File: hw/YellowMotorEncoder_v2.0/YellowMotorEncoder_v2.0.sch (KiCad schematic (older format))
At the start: 30 parts, among them J1 Conn_01x06, Q1 AO3401A, U1 47k, U10 10k, U11 47k, U12 18p/50V, U13 BLUE, U14 10k, U15 BLUE, U16 10k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

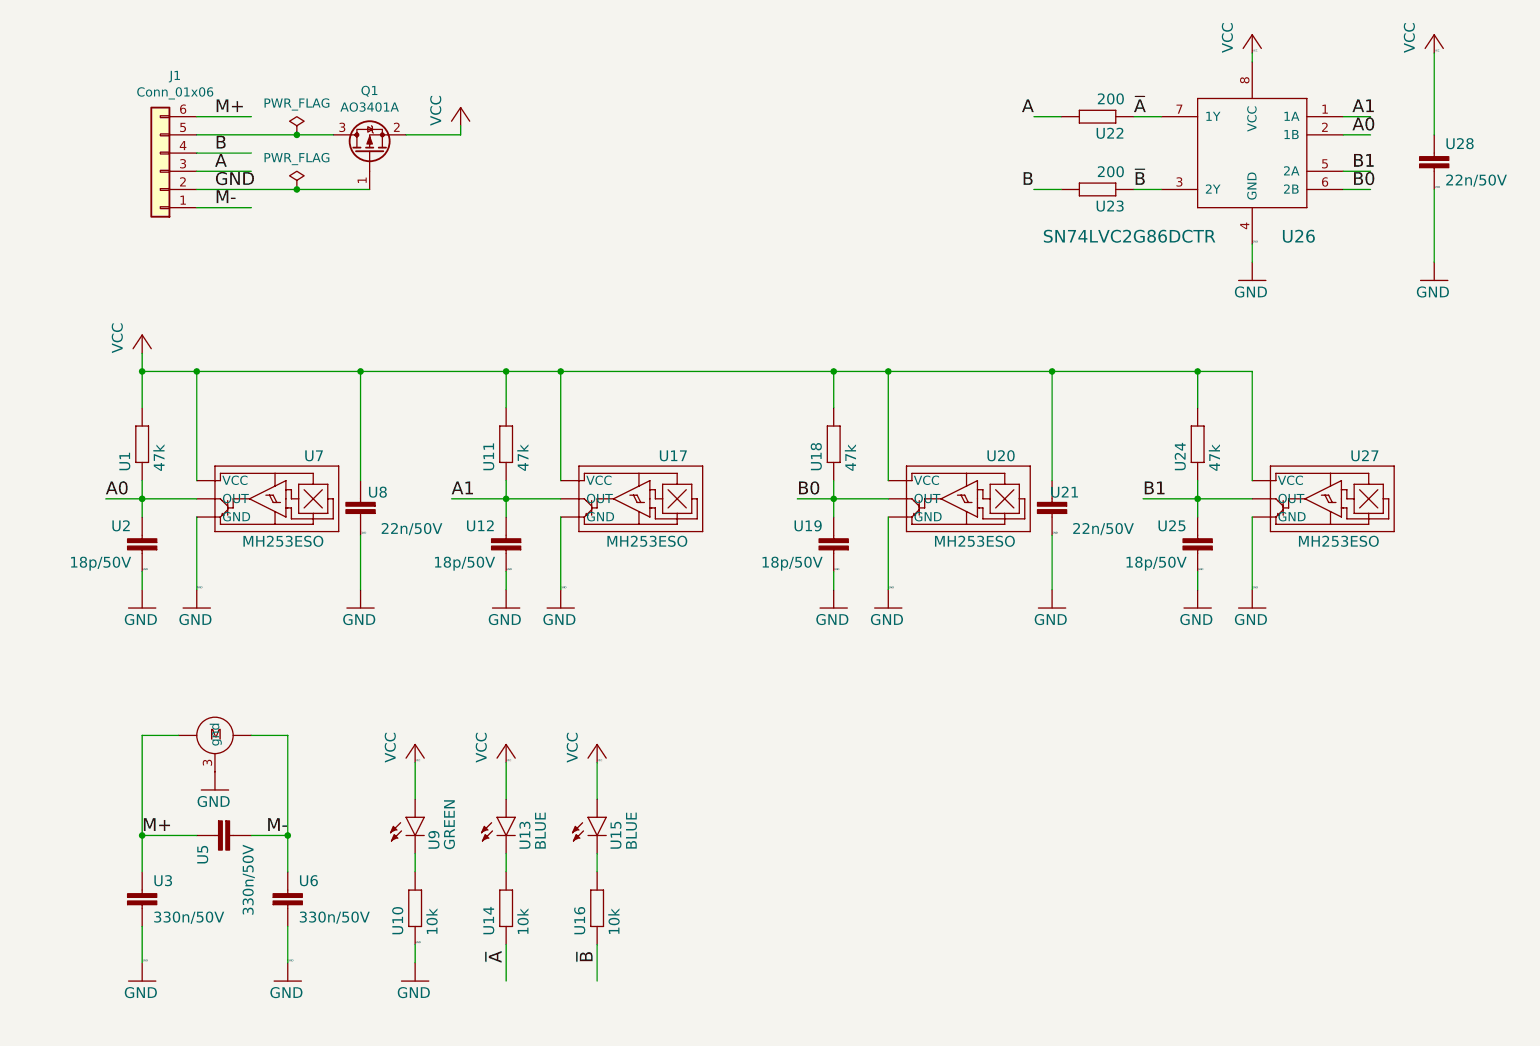
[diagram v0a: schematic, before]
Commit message: 3D_viewer
i add 3d model of motor and connector
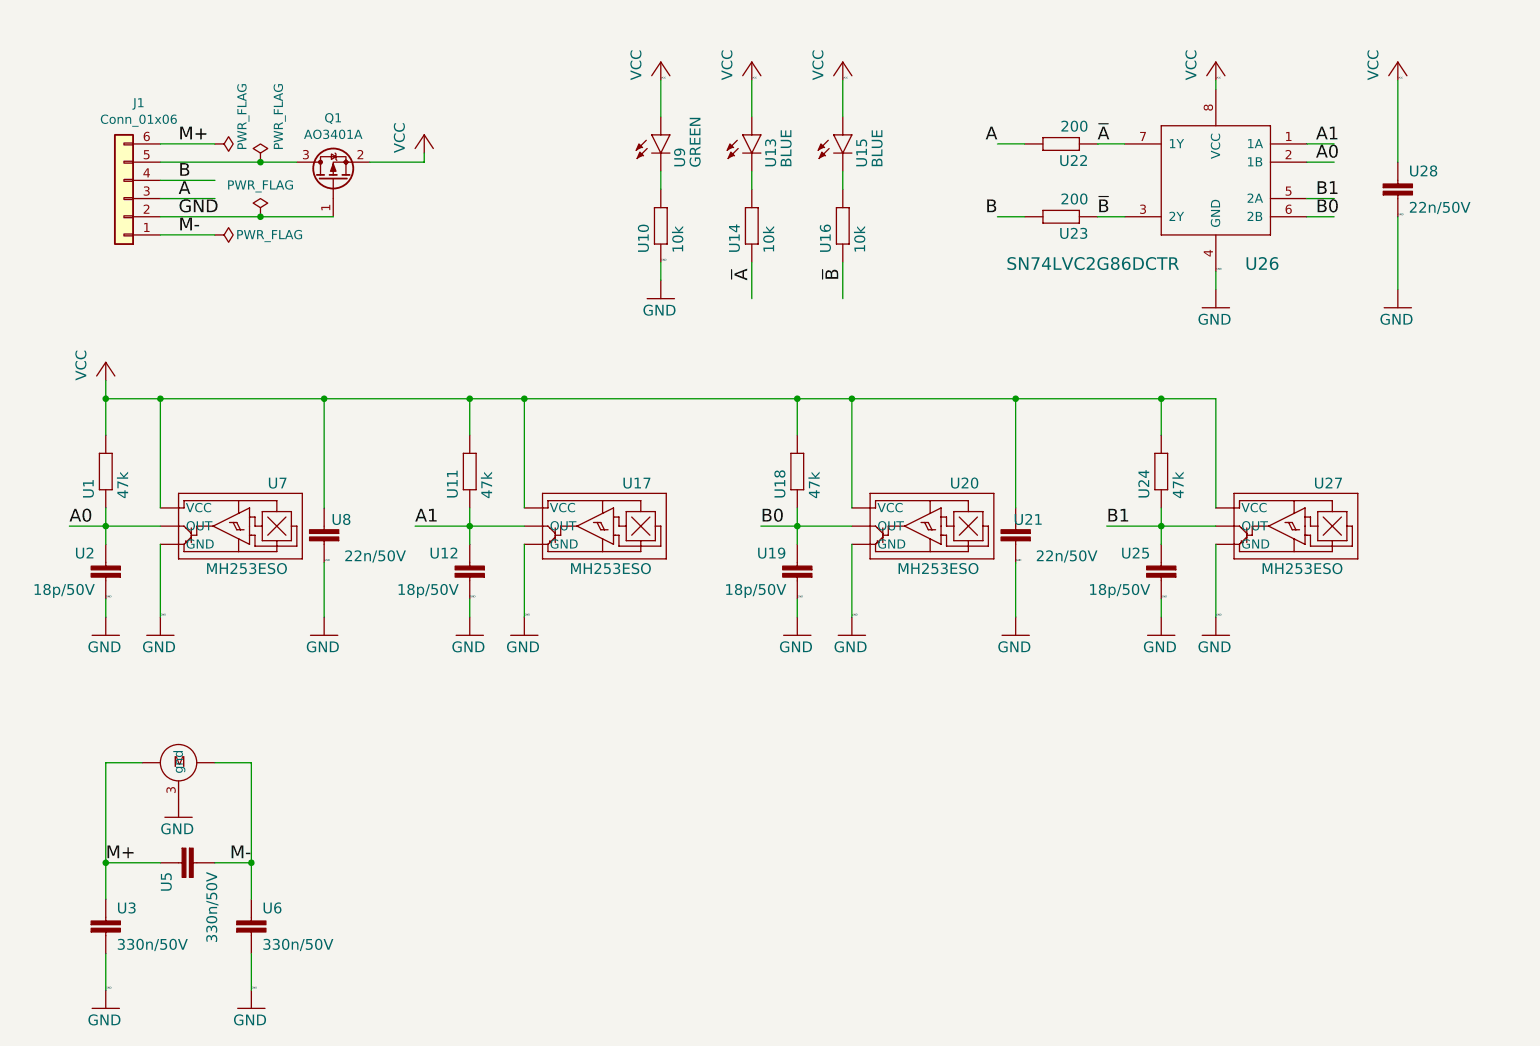
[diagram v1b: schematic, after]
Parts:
- U7: LCSC (none) -> C114369
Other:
- moved on the sheet: J1, Q1, U1, U10, U11, U12, U13, U14, U15, U16, U17, U18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

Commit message: rotate sensors
I changing position of sensors and rotating it in circle around hole for shaft of motor.
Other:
- moved on the sheet: U11, U12, U17, U18, U19, U20, U24, U25, U27
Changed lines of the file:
@@
 Wire Wire Line
 	6200 3950 6200 3850
-Wire Wire Line
-	6200 4050 6200 3950
 Text Label 6000 3950 0    70   ~ 0
 B0
@@
 L YellowMotorEncoder_v2.0-eagle-import:MH253ESO U27
 U 1 1 5F83AED4
-P 9100 3950
-F 0 "U27" H 9000 4150 59  0000 L BNN
-F 1 "MH253ESO" H 9000 3680 59  0000 L BNN
-F 2 "Package_TO_SOT_SMD:SOT-23" H 9100 3950 50  0001 C CNN
-F 3 "" H 9100 3950 50  0001 C CNN
-	1    9100 3950
+P 7100 3950
+F 0 "U27" H 7000 4150 59  0000 L BNN
+F 1 "MH253ESO" H 7000 3680 59  0000 L BNN
+F 2 "Package_TO_SOT_SMD:SOT-23" H 7100 3950 50  0001 C CNN
+F 3 "" H 7100 3950 50  0001 C CNN
+	1    7100 3950
 	-1   0    0    -1
 $EndComp
@@
 L YellowMotorEncoder_v2.0-eagle-import:R-EU_R0402 U24
 U 1 1 5F8679BE
-P 8200 3650
-F 0 "U24" H 8050 3709 59  0000 L BNN
-F 1 "47k" H 8050 3520 59  0000 L BNN
-F 2 "Resistor_SMD:R_0402_1005Metric" H 8200 3650 50  0001 C CNN
-F 3 "" H 8200 3650 50  0001 C CNN
-F 4 "C25792" H 8200 3650 59  0001 L BNN "LCSC"
-	1    8200 3650
+P 6200 3650
+F 0 "U24" H 6050 3709 59  0000 L BNN
+F 1 "47k" H 6050 3520 59  0000 L BNN
+F 2 "Resistor_SMD:R_0402_1005Metric" H 6200 3650 50  0001 C CNN
+F 3 "" H 6200 3650 50  0001 C CNN
+F 4 "C25792" H 6200 3650 59  0001 L BNN "LCSC"
+	1    6200 3650
 	0    -1   -1   0
 $EndComp
@@
 L YellowMotorEncoder_v2.0-eagle-import:MH253ESO U20
 U 1 1 5F86AC81
-P 7100 3950
-F 0 "U20" H 7000 4150 59  0000 L BNN
-F 1 "MH253ESO" H 7000 3680 59  0000 L BNN
-F 2 "Package_TO_SOT_SMD:SOT-23" H 7100 3950 50  0001 C CNN
-F 3 "" H 7100 3950 50  0001 C CNN
-	1    7100 3950
-	-1   0    0    -1
-$EndComp
-$Comp
-L YellowMotorEncoder_v2.0-eagle-import:MH253ESO U17
-U 1 1 5F86BD7E
 P 5300 3950
-F 0 "U17" H 5200 4150 59  0000 L BNN
+F 0 "U20" H 5200 4150 59  0000 L BNN
 F 1 "MH253ESO" H 5200 3680 59  0000 L BNN
 F 2 "Package_TO_SOT_SMD:SOT-23" H 5300 3950 50  0001 C CNN
 F 3 "" H 5300 3950 50  0001 C CNN
 	1    5300 3950
+	-1   0    0    -1
+$EndComp
+$Comp
+L YellowMotorEncoder_v2.0-eagle-import:MH253ESO U17
+U 1 1 5F86BD7E
+P 9100 3950
+F 0 "U17" H 9000 4150 59  0000 L BNN
+F 1 "MH253ESO" H 9000 3680 59  0000 L BNN
+F 2 "Package_TO_SOT_SMD:SOT-23" H 9100 3950 50  0001 C CNN
+F 3 "" H 9100 3950 50  0001 C CNN
+	1    9100 3950
 	-1   0    0    -1
 $EndComp
@@
 L YellowMotorEncoder_v2.0-eagle-import:C-EUC0402 U12
 U 1 1 5F8749CE
+P 8200 4150
+F 0 "U12" H 8260 4165 59  0000 L BNN
+F 1 "18p/50V" H 8260 3965 59  0000 L BNN
+F 2 "Capacitor_SMD:C_0402_1005Metric" H 8200 4150 50  0001 C CNN
+F 3 "" H 8200 4150 50  0001 C CNN
+F 4 "C1549" H 8200 4150 59  0001 L BNN "LCSC"
+	1    8200 4150
+	-1   0    0    -1
+$EndComp
+$Comp
+L YellowMotorEncoder_v2.0-eagle-import:C-EUC0402 U19
+U 1 1 5F8754D9
 P 4400 4150
-F 0 "U12" H 4460 4165 59  0000 L BNN
+F 0 "U19" H 4460 4165 59  0000 L BNN
 F 1 "18p/50V" H 4460 3965 59  0000 L BNN
 F 2 "Capacitor_SMD:C_0402_1005Metric" H 4400 4150 50  0001 C CNN
@@
 F 4 "C1549" H 4400 4150 59  0001 L BNN "LCSC"
 	1    4400 4150
-	-1   0    0    -1
-$EndComp
-$Comp
-L YellowMotorEncoder_v2.0-eagle-import:C-EUC0402 U19
-U 1 1 5F8754D9
-P 6200 4150
-F 0 "U19" H 6260 4165 59  0000 L BNN
-F 1 "18p/50V" H 6260 3965 59  0000 L BNN
-F 2 "Capacitor_SMD:C_0402_1005Metric" H 6200 4150 50  0001 C CNN
-F 3 "" H 6200 4150 50  0001 C CNN
-F 4 "C1549" H 6200 4150 59  0001 L BNN "LCSC"
-	1    6200 4150
-	-1   0    0    -1
-$EndComp
-$Comp
-L YellowMotorEncoder_v2.0-eagle-import:C-EUC0402 U25
-U 1 1 5F876094
-P 8200 4150
-F 0 "U25" H 8260 4165 59  0000 L BNN
-F 1 "18p/50V" H 8260 3965 59  0000 L BNN
-F 2 "Capacitor_SMD:C_0402_1005Metric" H 8200 4150 50  0001 C CNN
-F 3 "" H 8200 4150 50  0001 C CNN
-F 4 "C1549" H 8200 4150 59  0001 L BNN "LCSC"
-	1    8200 4150
 	-1   0    0    -1
 $EndComp
@@
 L YellowMotorEncoder_v2.0-eagle-import:R-EU_R0402 U18
 U 1 1 5F8A9DF8
-P 6200 3650
-F 0 "U18" H 6050 3709 59  0000 L BNN
-F 1 "47k" H 6050 3520 59  0000 L BNN
-F 2 "Resistor_SMD:R_0402_1005Metric" H 6200 3650 50  0001 C CNN
-F 3 "" H 6200 3650 50  0001 C CNN
-F 4 "C25792" H 6200 3650 59  0001 L BNN "LCSC"
-	1    6200 3650
-	0    -1   -1   0
-$EndComp
-$Comp
-L YellowMotorEncoder_v2.0-eagle-import:R-EU_R0402 U11
-U 1 1 5F8AAAB3
 P 4400 3650
-F 0 "U11" H 4250 3709 59  0000 L BNN
+F 0 "U18" H 4250 3709 59  0000 L BNN
 F 1 "47k" H 4250 3520 59  0000 L BNN
 F 2 "Resistor_SMD:R_0402_1005Metric" H 4400 3650 50  0001 C CNN
@@
 F 4 "C25792" H 4400 3650 59  0001 L BNN "LCSC"
 	1    4400 3650
+	0    -1   -1   0
+$EndComp
+$Comp
+L YellowMotorEncoder_v2.0-eagle-import:R-EU_R0402 U11
+U 1 1 5F8AAAB3
+P 8200 3650
+F 0 "U11" H 8050 3709 59  0000 L BNN
+F 1 "47k" H 8050 3520 59  0000 L BNN
+F 2 "Resistor_SMD:R_0402_1005Metric" H 8200 3650 50  0001 C CNN
+F 3 "" H 8200 3650 50  0001 C CNN
+F 4 "C25792" H 8200 3650 59  0001 L BNN "LCSC"
+	1    8200 3650
 	0    -1   -1   0
 $EndComp
@@
 	0    1    1    0
 $EndComp
+Wire Wire Line
+	6200 4050 6200 3950
+$Comp
+L YellowMotorEncoder_v2.0-eagle-import:C-EUC0402 U25
+U 1 1 5F876094
+P 6200 4150
+F 0 "U25" H 6260 4165 59  0000 L BNN
+F 1 "18p/50V" H 6260 3965 59  0000 L BNN
+F 2 "Capacitor_SMD:C_0402_1005Metric" H 6200 4150 50  0001 C CNN
+F 3 "" H 6200 4150 50  0001 C CNN
+F 4 "C1549" H 6200 4150 59  0001 L BNN "LCSC"
+	1    6200 4150
+	-1   0    0    -1
+$EndComp
 $EndSCHEMATC
